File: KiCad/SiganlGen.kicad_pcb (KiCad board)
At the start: 2 copper layers, 74 parts, among them J1 Barrel_Jack_MountingPin, J2 Conn_Coaxial, J3 PWR, J4 Btn_Matrix, J5 Enc_Conn, J7 Btn&Led, J8 LCD_Conn, Q3 BD135, Q4 BD136, U1 RaspberryPi_Pico, U2 LM7805_TO220, U4 LM337_TO220, U5 LM318H, U6 MC34063AP, U7 LM7810_TO220

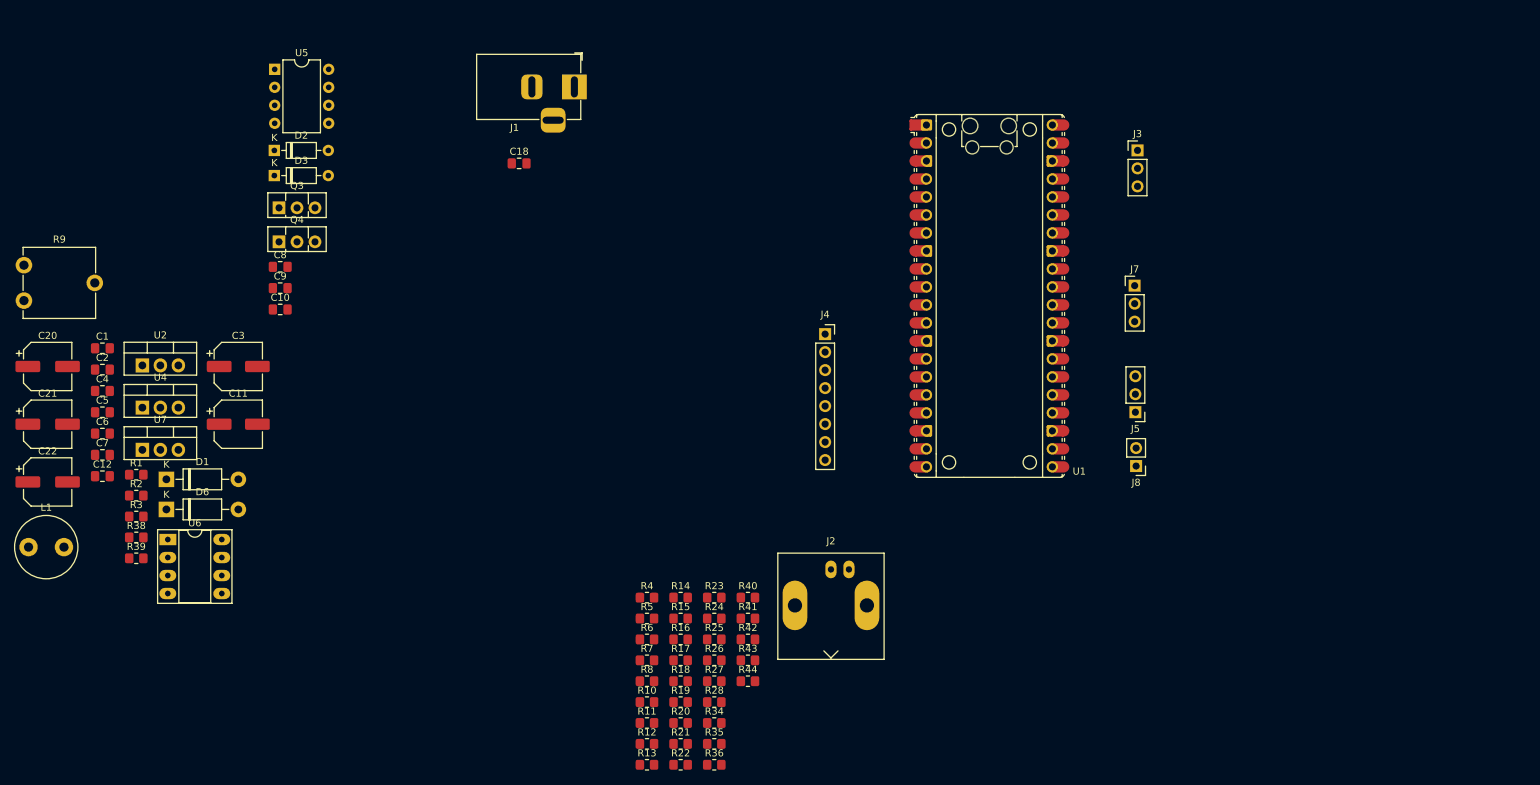
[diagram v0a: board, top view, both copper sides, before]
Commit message: First DAC layout, rough board layout
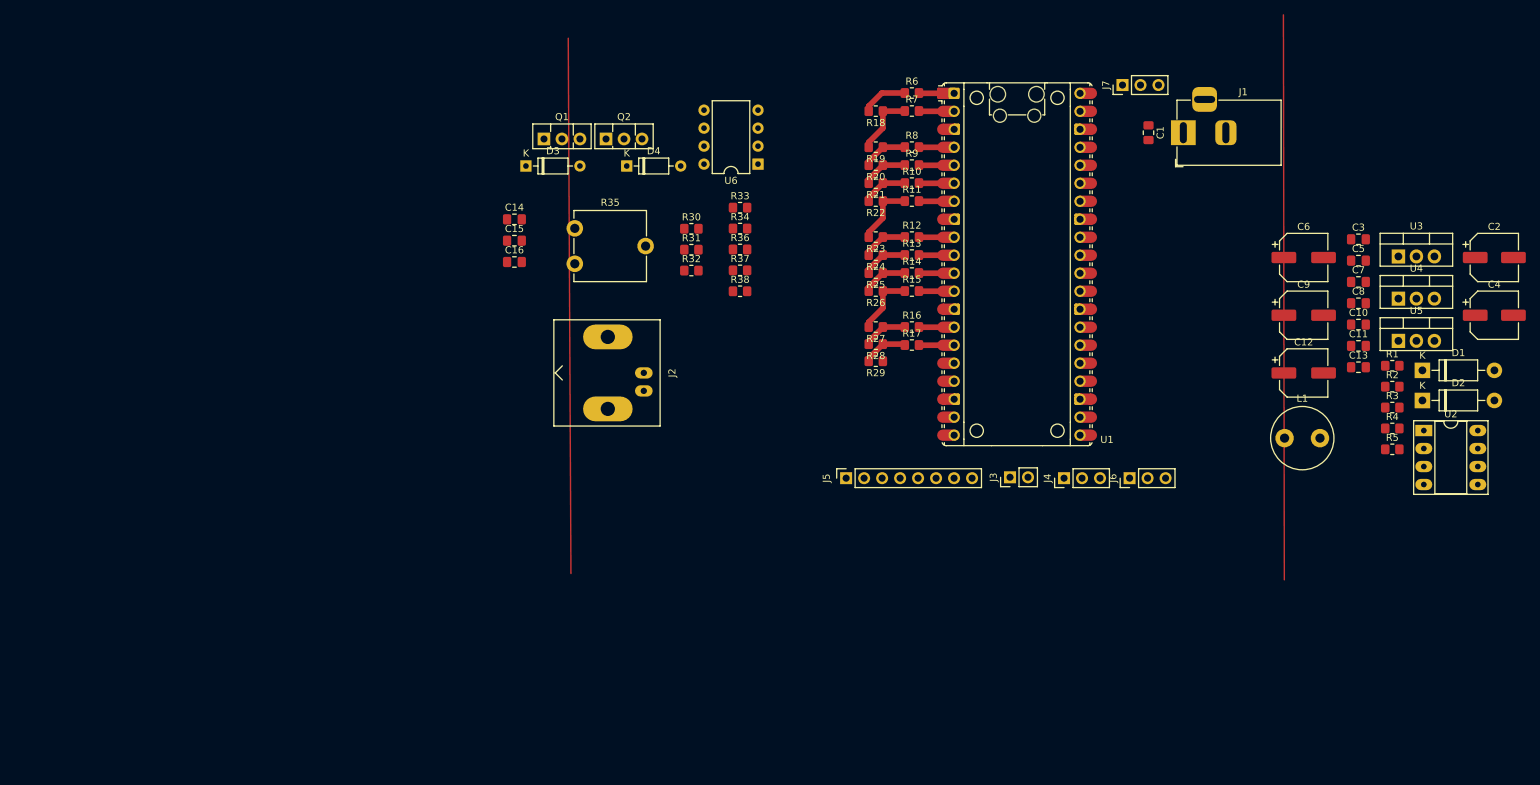
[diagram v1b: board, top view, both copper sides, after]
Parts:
- removed C18: 100n, Capacitor_SMD:C_0805_2012Metric_Pad1.18x1.45mm_HandSolder
- removed C20, C21, C22: 22u, Capacitor_SMD:CP_Elec_6.3x5.3
- removed D6: 1N4007, Diode_THT:D_DO-41_SOD81_P10.16mm_Horizontal
- removed J8: LCD_Conn, Connector_PinHeader_2.54mm:PinHeader_1x02_P2.54mm_Vertical
- removed Q3: BD135, Package_TO_SOT_THT:TO-126-3_Vertical
- removed Q4: BD136, Package_TO_SOT_THT:TO-126-3_Vertical
- removed R39: 860, Resistor_SMD:R_0805_2012Metric_Pad1.20x1.40mm_HandSolder
- removed R40, R42, R44: 1k, Resistor_SMD:R_0805_2012Metric_Pad1.20x1.40mm_HandSolder
- removed R41, R43: 2k, Resistor_SMD:R_0805_2012Metric_Pad1.20x1.40mm_HandSolder
- removed U7: LM7810_TO220, Package_TO_SOT_THT:TO-220-3_Vertical
- added C13: 100n, Capacitor_SMD:C_0805_2012Metric_Pad1.18x1.45mm_HandSolder, F.Cu at (205.8, 81.9)
- added C14: 3,3p, Capacitor_SMD:C_0805_2012Metric_Pad1.18x1.45mm_HandSolder, F.Cu at (86.6, 61.0)
- added C15: 100n, Capacitor_SMD:C_0805_2012Metric_Pad1.18x1.45mm_HandSolder, F.Cu at (86.6, 64.0)
- added C16: 100n, Capacitor_SMD:C_0805_2012Metric_Pad1.18x1.45mm_HandSolder, F.Cu at (86.6, 67.0)
- added D4: 1N4148, Diode_THT:D_DO-35_SOD27_P7.62mm_Horizontal, F.Cu at (102.5, 53.5)
- added J6: Btn&Led, Connector_PinHeader_2.54mm:PinHeader_1x03_P2.54mm_Vertical, F.Cu at (173.5, 97.5)
- added Q1: BD135, Package_TO_SOT_THT:TO-126-3_Vertical, F.Cu at (90.8, 49.7)
- added Q2: BD136, Package_TO_SOT_THT:TO-126-3_Vertical, F.Cu at (99.6, 49.7)
- added R29: 1k, Resistor_SMD:R_0805_2012Metric_Pad1.20x1.40mm_HandSolder, F.Cu at (137.7, 81.0)
- added R30: 20k, Resistor_SMD:R_0805_2012Metric_Pad1.20x1.40mm_HandSolder, F.Cu at (111.6, 62.3)
- added R31: 680, Resistor_SMD:R_0805_2012Metric_Pad1.20x1.40mm_HandSolder, F.Cu at (111.6, 65.3)
- added R32: 680, Resistor_SMD:R_0805_2012Metric_Pad1.20x1.40mm_HandSolder, F.Cu at (111.6, 68.2)
- added R33: 27, Resistor_SMD:R_0805_2012Metric_Pad1.20x1.40mm_HandSolder, F.Cu at (118.5, 59.3)
- added R37: 3,3, Resistor_SMD:R_0805_2012Metric_Pad1.20x1.40mm_HandSolder, F.Cu at (118.5, 68.2)
- added U3: LM7805_TO220, Package_TO_SOT_THT:TO-220-3_Vertical, F.Cu at (211.4, 66.2)
- C10: value 3,3p -> 330n
- C11: value 220u -> 100n; footprint Capacitor_SMD:CP_Elec_6.3x7.7 -> Capacitor_SMD:C_0805_2012Metric_Pad1.18x1.45mm_HandSolder
- C12, C6, C9: value 100n -> 22u; footprint Capacitor_SMD:C_0805_2012Metric_Pad1.18x1.45mm_HandSolder -> Capacitor_SMD:CP_Elec_6.3x5.3
- C2: value 100n -> 220u; footprint Capacitor_SMD:C_0805_2012Metric_Pad1.18x1.45mm_HandSolder -> Capacitor_SMD:CP_Elec_6.3x7.7
- C3: value 220u -> 470p; footprint Capacitor_SMD:CP_Elec_6.3x7.7 -> Capacitor_SMD:C_0805_2012Metric_Pad1.18x1.45mm_HandSolder
- C4: value 470p -> 220u; footprint Capacitor_SMD:C_0805_2012Metric_Pad1.18x1.45mm_HandSolder -> Capacitor_SMD:CP_Elec_6.3x7.7
- C7: value 330n -> 100n
- D2: value 1N4148 -> 1N4007; footprint Diode_THT:D_DO-35_SOD27_P7.62mm_Horizontal -> Diode_THT:D_DO-41_SOD81_P10.16mm_Horizontal
- J3: value PWR -> LCD_Conn; footprint Connector_PinHeader_2.54mm:PinHeader_1x03_P2.54mm_Vertical -> Connector_PinHeader_2.54mm:PinHeader_1x02_P2.54mm_Vertical
- J4: value Btn_Matrix -> Enc_Conn; footprint Connector_PinSocket_2.54mm:PinSocket_1x08_P2.54mm_Vertical -> Connector_PinHeader_2.54mm:PinHeader_1x03_P2.54mm_Vertical
- J5: value Enc_Conn -> Btn_Matrix; footprint Connector_PinHeader_2.54mm:PinHeader_1x03_P2.54mm_Vertical -> Connector_PinSocket_2.54mm:PinSocket_1x08_P2.54mm_Vertical
- J7: value Btn&Led -> PWR
- R10, R8: value 1k -> 2k
- R11, R12: value 3,3 -> 2k
- R18, R19, R20, R34, R36: value 2k -> 1k
- R35: value 1k -> 100; footprint Resistor_SMD:R_0805_2012Metric_Pad1.20x1.40mm_HandSolder -> Potentiometer_THT:Potentiometer_ACP_CA9-V10_Vertical
- R38: value 100 -> 3,3
- R4: value 20k -> 860
- R5: value 680 -> 100
- R6: value 680 -> 2k
- R7: value 27 -> 2k
- R9: value 100 -> 2k; footprint Potentiometer_THT:Potentiometer_ACP_CA9-V10_Vertical -> Resistor_SMD:R_0805_2012Metric_Pad1.20x1.40mm_HandSolder
- U2: value LM7805_TO220 -> MC34063AP; footprint Package_TO_SOT_THT:TO-220-3_Vertical -> Package_DIP:DIP-8_W7.62mm_Socket_LongPads
- U5: value LM318H -> LM7810_TO220; footprint Package_DIP:DIP-8_W7.62mm -> Package_TO_SOT_THT:TO-220-3_Vertical
- U6: value MC34063AP -> LM318H; footprint Package_DIP:DIP-8_W7.62mm_Socket_LongPads -> Package_DIP:DIP-8_W7.62mm
- moved C2 197.1 mm to (225.0, 66.4)
- moved C4 196.8 mm to (225.0, 74.5)
- moved U2 181.1 mm to (215.0, 90.8)
- moved C7 179.0 mm to (205.8, 69.8)
- moved C5 178.6 mm to (205.8, 66.8)
- moved U4 178.0 mm to (211.4, 72.2)
- moved D1 178.0 mm to (214.8, 82.3)
- moved L1 178.0 mm to (195.4, 91.9)
- moved R1 178.0 mm to (210.6, 81.7)
- moved R2 178.0 mm to (210.6, 84.6)
- moved R3 178.0 mm to (210.6, 87.6)
- moved C6 171.4 mm to (198.1, 66.4)
- moved C12 170.2 mm to (198.1, 82.7)
- moved D2 165.9 mm to (214.8, 86.6)
- moved U5 163.2 mm to (211.4, 78.2)
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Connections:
- C1 pad 1: GND -> +5V
- C1 pad 2: -12V -> GND
- C10 pad 1: /Output Stage/DAC_OUT -> +12V
- C11 pad 2: -12V -> -10V
- C12 pad 1: +10V -> GND
- C12 pad 2: GND -> -10V
- C3 pad 1: +12V -> Net-(U2-TC)
- C3 pad 2: GND -> -12V
- C4 pad 1: Net-(U6-TC) -> GND
- C5 pad 1: +5V -> +12V
- C6 pad 2: -10V -> -12V
- C7 pad 1: +12V -> GND
- C7 pad 2: GND -> -12V
- C8 pad 1: +10V -> +5V
- C9 pad 2: -10V -> Net-(U4-ADJ)
- D2 pad 1: Net-(D2-K) -> -10V
- D2 pad 2: Net-(D2-A) -> -12V
- J3 pad 1: +5V -> /LCD_SDA
- J3 pad 2: +3V3 -> /LCD_SCL
- J4 pad 1: /X0 -> /ENC_CLK
- J4 pad 2: /X1 -> /ENC_DT
- J4 pad 3: /X2 -> /ENC_SW
- J5 pad 1: /ENC_CLK -> /X0
- J5 pad 2: /ENC_DT -> /X1
- J5 pad 3: /ENC_SW -> /X2
- J7 pad 1: /SW1_OUT -> +5V
- J7 pad 2: /SW2_OUT -> +3V3
- J7 pad 3: /LED1_IN -> GND
- R1 pad 2: Net-(U6-DC) -> Net-(U2-DC)
- R10 pad 1: -10V -> Net-(R10-Pad1)
- R10 pad 2: Net-(D3-K) -> /DAC4
- R11 pad 1: Net-(J2-In) -> Net-(R11-Pad1)
- R11 pad 2: Net-(Q3-E) -> /DAC5
- R12 pad 1: Net-(Q4-E) -> Net-(R12-Pad1)
- R12 pad 2: Net-(J2-In) -> /DAC6
- R13 pad 1: /Output Stage/DAC_OUT -> Net-(R13-Pad1)
- R13 pad 2: /DAC0 -> /DAC7
- R14 pad 2: /DAC1 -> /X0
- R15 pad 2: /DAC2 -> /X1
- R16 pad 2: /DAC3 -> /X2
- R17 pad 2: /DAC4 -> /X3
- R18 pad 2: /DAC5 -> /Output Stage/DAC_OUT
- R19 pad 2: /DAC6 -> Net-(R18-Pad1)
- R2 pad 2: Net-(U6-Vfb) -> Net-(U2-Vfb)
- R20 pad 2: /DAC7 -> Net-(R19-Pad1)
- R21 pad 1: Net-(R14-Pad1) -> Net-(R10-Pad1)
- R21 pad 2: /Output Stage/DAC_OUT -> Net-(R20-Pad1)
- R22 pad 1: Net-(R15-Pad1) -> Net-(R11-Pad1)
- R22 pad 2: Net-(R14-Pad1) -> Net-(R10-Pad1)
- R23 pad 1: Net-(R16-Pad1) -> Net-(R12-Pad1)
- R23 pad 2: Net-(R15-Pad1) -> Net-(R11-Pad1)
- R24 pad 1: Net-(R17-Pad1) -> Net-(R13-Pad1)
- R24 pad 2: Net-(R16-Pad1) -> Net-(R12-Pad1)
- R25 pad 1: Net-(R18-Pad1) -> Net-(R14-Pad1)
- R25 pad 2: Net-(R17-Pad1) -> Net-(R13-Pad1)
- R26 pad 1: Net-(R19-Pad1) -> Net-(R15-Pad1)
- R26 pad 2: Net-(R18-Pad1) -> Net-(R14-Pad1)
- R27 pad 1: Net-(R20-Pad1) -> Net-(R16-Pad1)
- R27 pad 2: Net-(R19-Pad1) -> Net-(R15-Pad1)
- R28 pad 1: Net-(R28-Pad1) -> Net-(R17-Pad1)
- R28 pad 2: Net-(R20-Pad1) -> Net-(R16-Pad1)
- R3 pad 1: Net-(U6-Vfb) -> Net-(U2-Vfb)
- R34 pad 1: Net-(R28-Pad1) -> Net-(D3-A)
- R34 pad 2: /X0 -> +10V
- R35 pad 1: Net-(R35-Pad1) -> Net-(D3-K)
- R35 pad 2: Net-(R28-Pad1) -> Net-(D4-A)
- R36 pad 1: Net-(R35-Pad1) -> -10V
- R36 pad 2: /X1 -> Net-(D4-K)
- R38 pad 1: -10V -> Net-(Q2-E)
- R38 pad 2: Net-(U4-ADJ) -> Net-(J2-In)
- R4 pad 1: GND -> Net-(U4-ADJ)
- R4 pad 2: /Output Stage/DAC_OUT -> GND
- R5 pad 1: GND -> -10V
- R5 pad 2: Net-(U5--) -> Net-(U4-ADJ)
- R6 pad 1: Net-(U5--) -> /Output Stage/DAC_OUT
- R6 pad 2: Net-(R6-Pad2) -> /DAC0
- R7 pad 1: Net-(R6-Pad2) -> Net-(R18-Pad1)
- R7 pad 2: Net-(D2-K) -> /DAC1
- R8 pad 1: Net-(D2-A) -> Net-(R19-Pad1)
- R8 pad 2: +10V -> /DAC2
- R9 pad 1: Net-(D2-K) -> Net-(R20-Pad1)
- R9 pad 2: Net-(D3-A) -> /DAC3
- U2 pad 1: +12V -> Net-(U2-DC)
- U2 pad 2: GND -> Net-(D1-K)
- U2 pad 3: +5V -> Net-(U2-TC)
- U5 pad 1: unconnected-(U5-BAL1-Pad1) -> +12V
- U5 pad 2: Net-(U5--) -> GND
- U5 pad 3: /Output Stage/DAC_OUT -> +10V
- U6 pad 1: Net-(U6-DC) -> unconnected-(U6-BAL1-Pad1)
- U6 pad 2: Net-(D1-K) -> Net-(U6--)
- U6 pad 3: Net-(U6-TC) -> /Output Stage/DAC_OUT
- U6 pad 4: -12V -> -10V
- U6 pad 5: Net-(U6-Vfb) -> unconnected-(U6-BAL3-Pad5)
- U6 pad 6: +12V -> Net-(R32-Pad2)
- U6 pad 7: Net-(U6-DC) -> +10V
- U6 pad 8: Net-(U6-DC) -> unconnected-(U6-BAL2-Pad8)
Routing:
- net Net-(R18-Pad1): track 0.00 -> 9.02 mm
- net Net-(R15-Pad1): track 0.00 -> 9.00 mm
- net Net-(R11-Pad1): track 0.00 -> 9.00 mm
- net /Output Stage/DAC_OUT: track 0.00 -> 6.56 mm
- net Net-(R14-Pad1): track 0.00 -> 6.46 mm
- net Net-(R12-Pad1): track 0.00 -> 6.46 mm
- net Net-(R20-Pad1): track 0.00 -> 6.46 mm
- net Net-(R10-Pad1): track 0.00 -> 6.46 mm
- net Net-(R13-Pad1): track 0.00 -> 6.46 mm
- net Net-(R19-Pad1): track 0.00 -> 6.46 mm
- net Net-(R17-Pad1): track 0.00 -> 6.39 mm
- net Net-(R16-Pad1): track 0.00 -> 6.34 mm
- net /DAC1: track 0.00 -> 4.98 mm
- net /DAC0: track 0.00 -> 4.98 mm
- net /X3: track 0.00 -> 4.97 mm
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
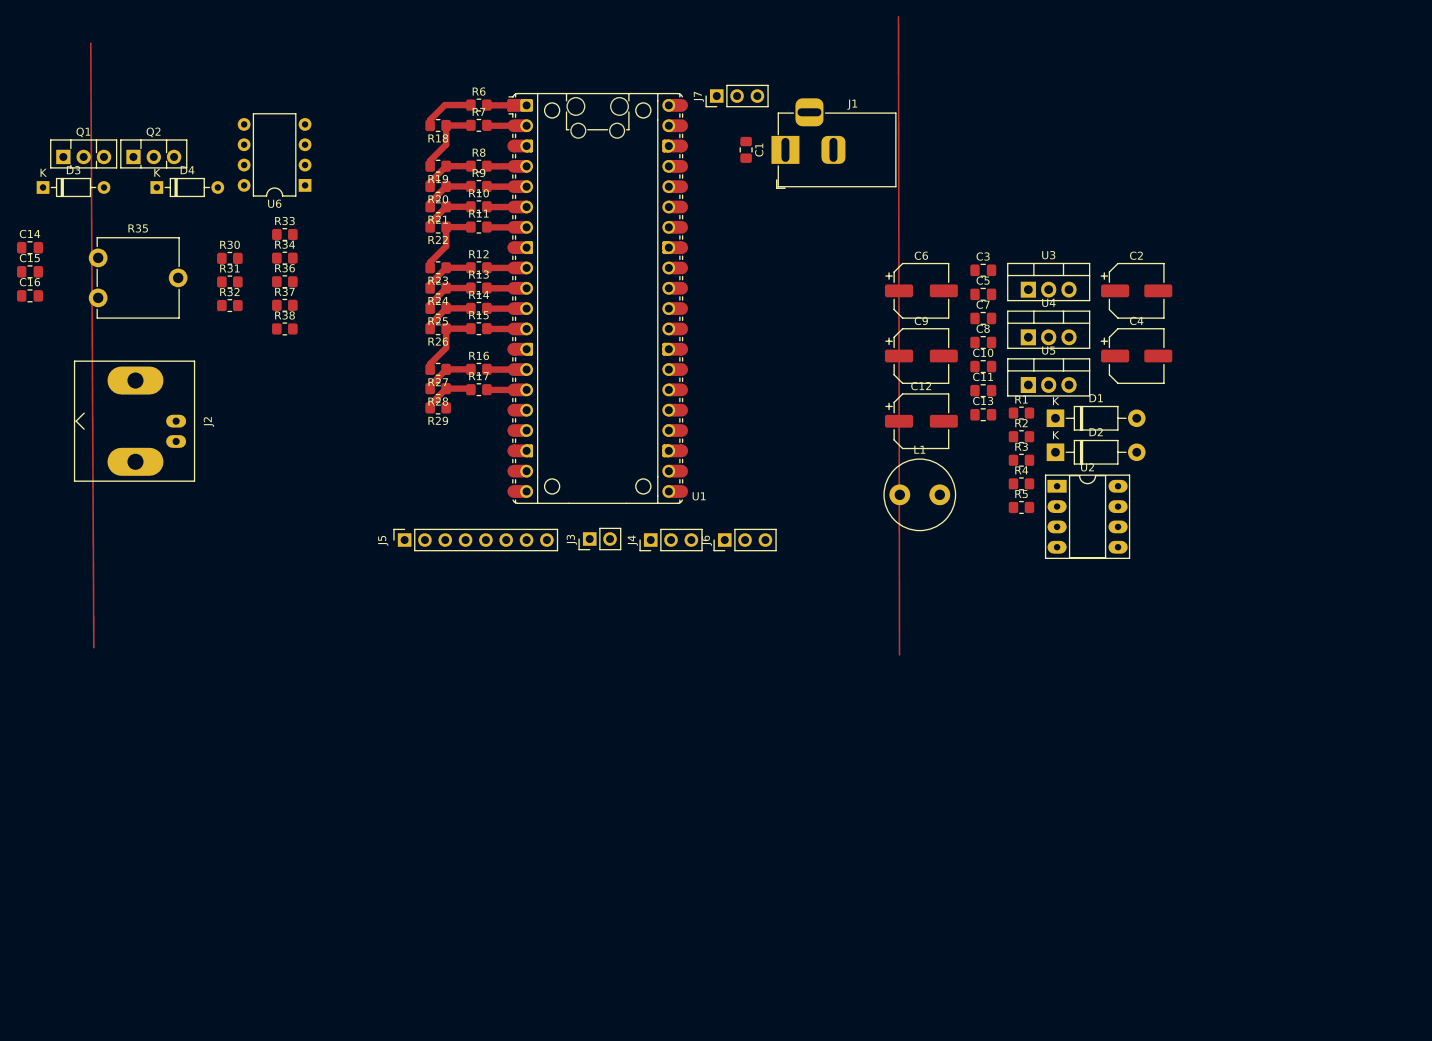
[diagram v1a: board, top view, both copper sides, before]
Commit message: bom, changed lm7810 to lm317
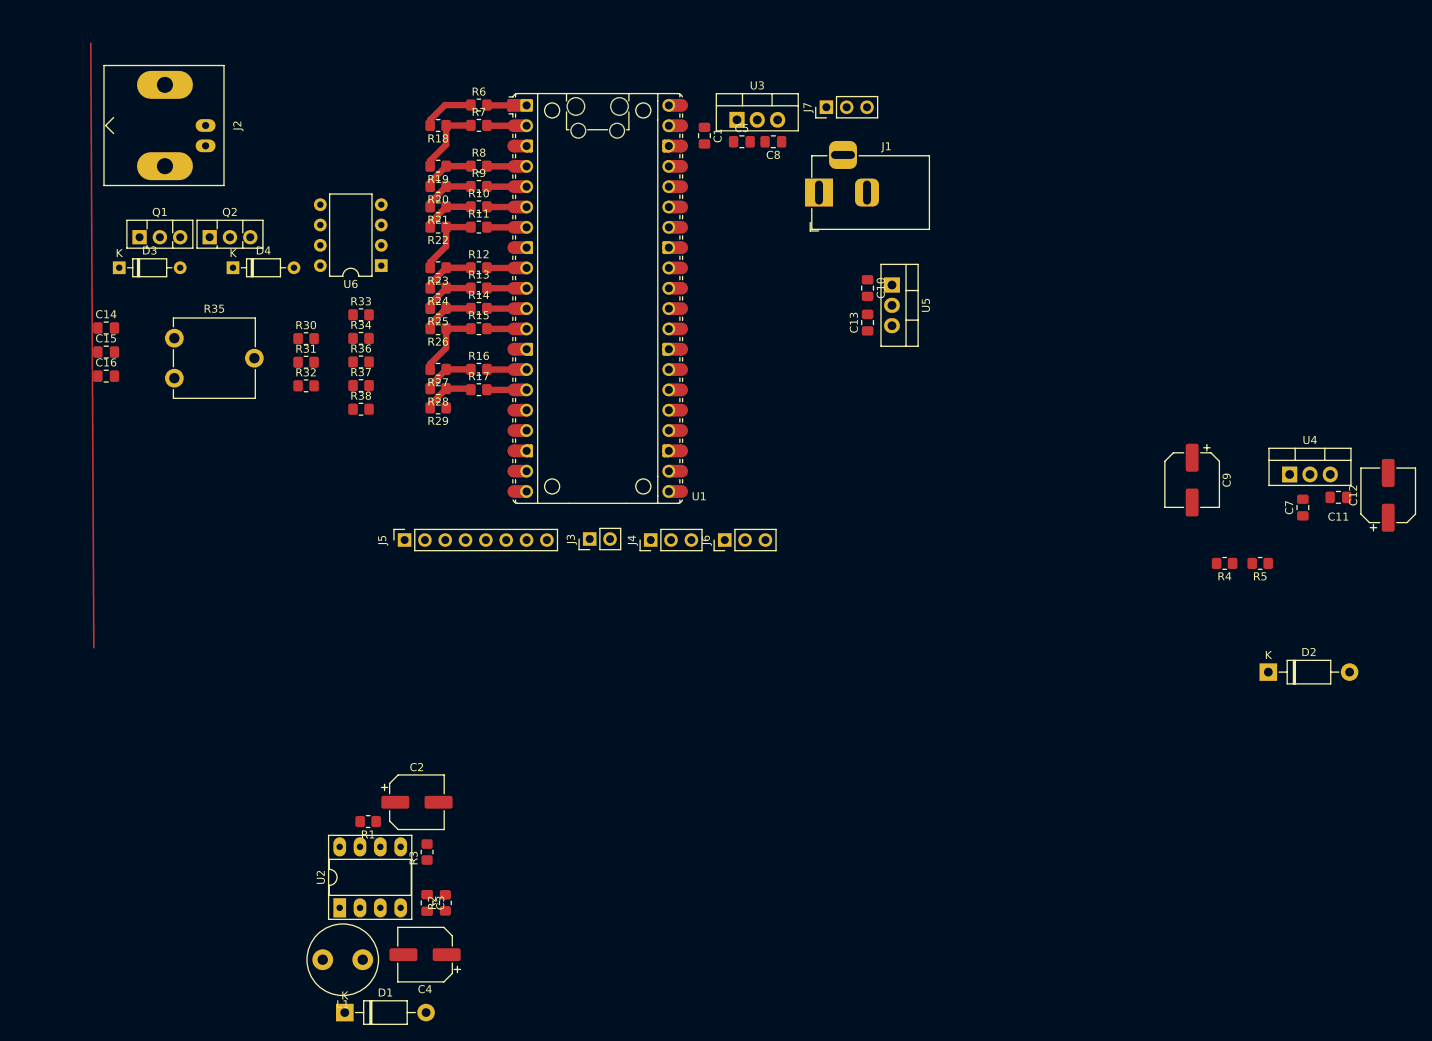
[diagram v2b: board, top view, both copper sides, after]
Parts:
- removed C6: 22u, Capacitor_SMD:CP_Elec_6.3x5.3
- moved C4 116.2 mm to (136.0, 149.4), turned to 180 degrees
- moved D1 115.8 mm to (126.0, 156.6)
- moved C2 110.4 mm to (135.0, 130.3)
- moved C3 105.3 mm to (136.3, 142.9), turned to -90 degrees
- moved U2 104.0 mm to (125.3, 143.5), turned to 90 degrees
- moved R1 96.3 mm to (128.9, 132.7), turned to 180 degrees
- moved R2 92.6 mm to (138.6, 142.9), turned to 90 degrees
- moved R3 89.0 mm to (136.3, 136.5), turned to 90 degrees
- moved L1 88.8 mm to (128.2, 150.0), turned to 180 degrees
- moved C12 59.1 mm to (256.4, 91.9), turned to 90 degrees
- moved C7 46.4 mm to (245.7, 93.5), turned to 90 degrees
- moved C11 46.4 mm to (250.2, 92.2), turned to 180 degrees
- moved U3 42.2 mm to (175.0, 45.0)
- moved D2 38.3 mm to (241.4, 114.0)
- moved C9 37.2 mm to (231.9, 90.0), turned to -90 degrees
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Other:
- board text added: "DC-DC inverter"
